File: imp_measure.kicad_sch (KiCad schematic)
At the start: 46 parts, among them IC1 DAC80501ZDGST, IC2 MAX660MX_NOPB, J1 Conn_01x04_Pin, J2 USB_B_Micro, J3 Conn_01x06_Pin, J4 Conn_01x06_Pin, SW1 SW_SPDT, U1 AMS1117-3.3, U2 STM32F401RCTx, U3 OPA196xDBV, Y1 26MHz

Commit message: PCB design 1.0
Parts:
- removed J3: Conn_01x06_Pin, Connector_PinHeader_2.54mm:PinHeader_1x04_P2.54mm_Vertical, symbol Connector:Conn_01x06_Pin
- removed U3: OPA196xDBV, Package_TO_SOT_SMD:SOT-23-5, symbol Amplifier_Operational:OPA196xDBV
- removed Y1: 26MHz, Crystal:Crystal_SMD_3225-4Pin_3.2x2.5mm, symbol Device:Crystal_GND23
- added C25: 100n, Capacitor_SMD:C_0805_2012Metric, symbol Device:C
- added C26, C27, C28, C30, C31: 1u, Capacitor_SMD:C_0805_2012Metric, symbol Device:C
- added C32: 10n, Capacitor_SMD:C_0805_2012Metric, symbol Device:C
- added FB3, FB4: 120R, Inductor_SMD:L_0805_2012Metric, symbol Device:FerriteBead
- added H1, H2, H3, H4: MountingHole, MountingHole:MountingHole_2mm, symbol Mechanical:MountingHole
- added IC4: MC33202DR2G, SamacSys_Parts:SOIC127P600X175-8N, symbol SamacSys_Parts:MC33202DR2G
- added J3, J5: Conn_01x04_Pin, Connector_PinHeader_2.54mm:PinHeader_1x04_P2.54mm_Vertical, symbol Connector:Conn_01x04_Pin
- added R9: 1k, Resistor_SMD:R_0805_2012Metric, symbol Device:R
- added Y1: Crystal, Crystal:Crystal_HC49-U_Vertical, symbol Device:Crystal
- C10, C11, C12, C13, C14, C15, C16, C17, C21, C22, C23, C4, C8, C9: footprint Capacitor_SMD:C_0402_1005Metric -> Capacitor_SMD:C_0805_2012Metric
- C18: value 100n -> 5n; footprint Capacitor_SMD:C_0402_1005Metric -> Capacitor_SMD:C_0805_2012Metric
- C19: value 100n -> 10n; footprint Capacitor_SMD:C_0402_1005Metric -> Capacitor_SMD:C_0805_2012Metric
- C3, C6, C7: footprint Capacitor_SMD:C_0603_1608Metric -> Capacitor_SMD:C_0805_2012Metric
- C5: value 100n -> 220n; footprint Capacitor_SMD:C_0402_1005Metric -> Capacitor_SMD:C_0805_2012Metric
- D1: footprint LED_SMD:LED_0603_1608Metric -> LED_SMD:LED_0805_2012Metric
- FB1, FB2: footprint Inductor_SMD:L_0603_1608Metric -> Inductor_SMD:L_0805_2012Metric
- R1, R2, R3, R4, R5: footprint Resistor_SMD:R_0402_1005Metric -> Resistor_SMD:R_0805_2012Metric
- R6, R7: value R -> 3k3; footprint Resistor_SMD:R_0402_1005Metric -> Resistor_SMD:R_0805_2012Metric
- R8: value R -> 1k6; footprint Resistor_SMD:R_0402_1005Metric -> Resistor_SMD:R_0805_2012Metric
- SW1: footprint Button_Switch_THT:SW_Slide_SPDT_Straight_CK_OS102011MS2Q -> Button_Switch_SMD:SW_SPDT_PCM12
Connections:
- net +3.3V: now also FB4.2; no longer C3.1, C4.1, C5.1, IC1.1 (VDD), IC1.10 (VREFIO)
- net +3.3VA: now also R9.1
- net ADC1_IN4: now also J3.3 (Pin_3)
- net ADC1_IN5: now also J3.2 (Pin_2)
- net DAC_OUT: now also J5.2 (Pin_2)
- net DAC_OUT_FILTERED: now also IC4.7 (OUTPUT_2), J5.3 (Pin_3)
- net GND: now also C27.2, C28.2, C30.2, C31.2, C32.2, IC4.3 (INPUTS_1_2), IC4.5 (INPUTS_2_1), J3.4 (Pin_4), J5.4 (Pin_4)
- net RCC_OSC_IN: now also Y1.1
- net RCC_OSC_OUT: now also Y1.2
- net VBUS: now also C3.1, C4.1, IC1.1 (VDD), C30.1, FB3.2
- net VBUS_M: now also C27.1
- net VBUS_MF: now also C25.2, IC4.4 (VEE)
- net at C18.1, R8.2: now also IC4.6 (INPUTS_2_2)
- net at C20.1, IC2.2 (CAP+): now also C26.1
- net at C20.2, IC2.4 (CAP-): now also C26.2
- new net: C5.1, IC1.10 (VREFIO), R9.2
- new net: IC4.1 (OUTPUT_1), IC4.2 (INPUTS_1_1)
- new net +3.3V_F: C28.1, FB4.1, J3.1 (Pin_1), J5.1 (Pin_1)
- new net VBUS_PF: C25.1, C31.1, C32.1, FB3.1, IC4.8 (VCC)
- no-connect marks 45 -> 44
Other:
- note added: "Butterworth low-pass"
- note added: "G(s) = -3787878787.8788/(s^2+123106.06s+3787878787.87788)"
- note added: "Mounting holes"
- note added: "VDDA filtering for OPAMP"
- note removed: "Butterworth low-pass components to be calculated"
- note removed: "Output stage?"
- moved on the sheet: C18, C19, C20, C21, C22, C23, C24, C3, C4, FB2, IC1, IC2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

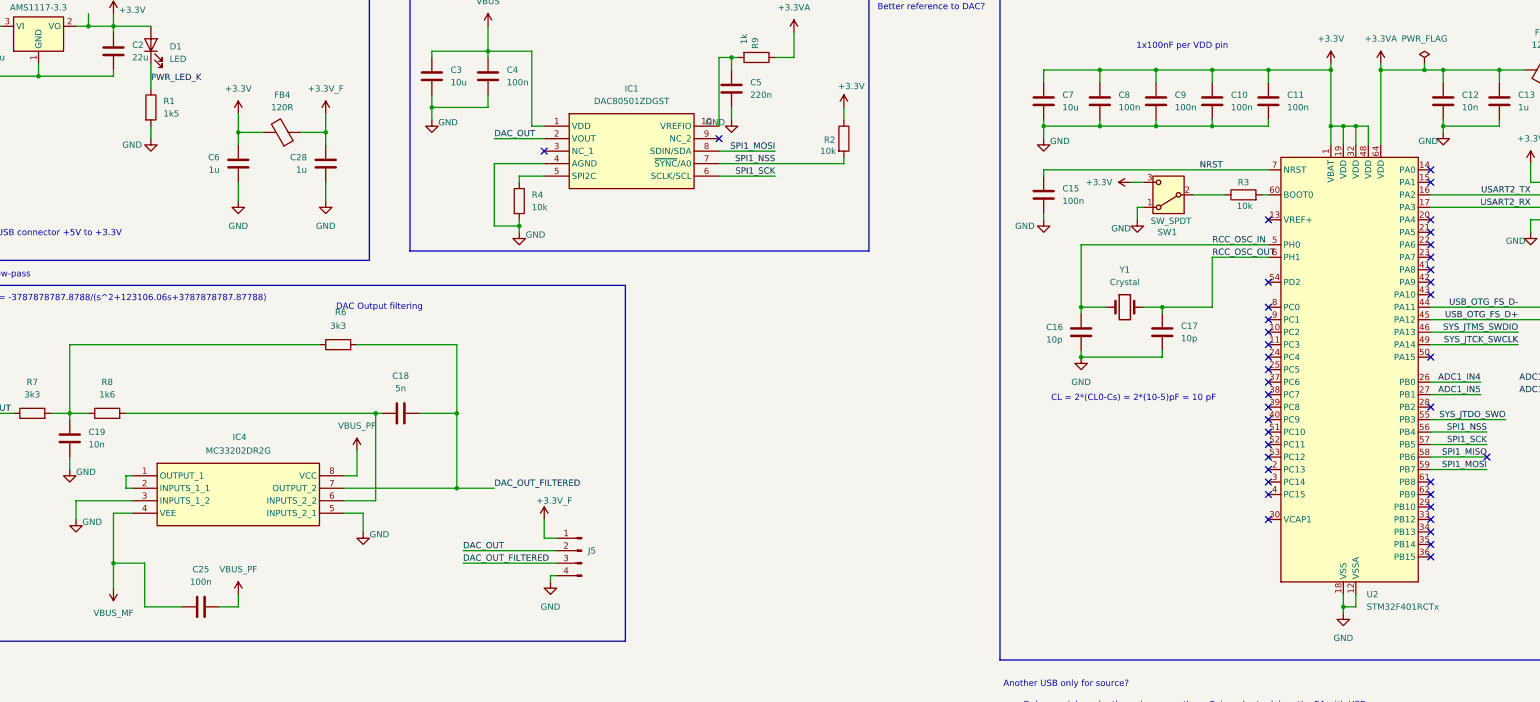
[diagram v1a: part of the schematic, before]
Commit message: Ground fill for analog part
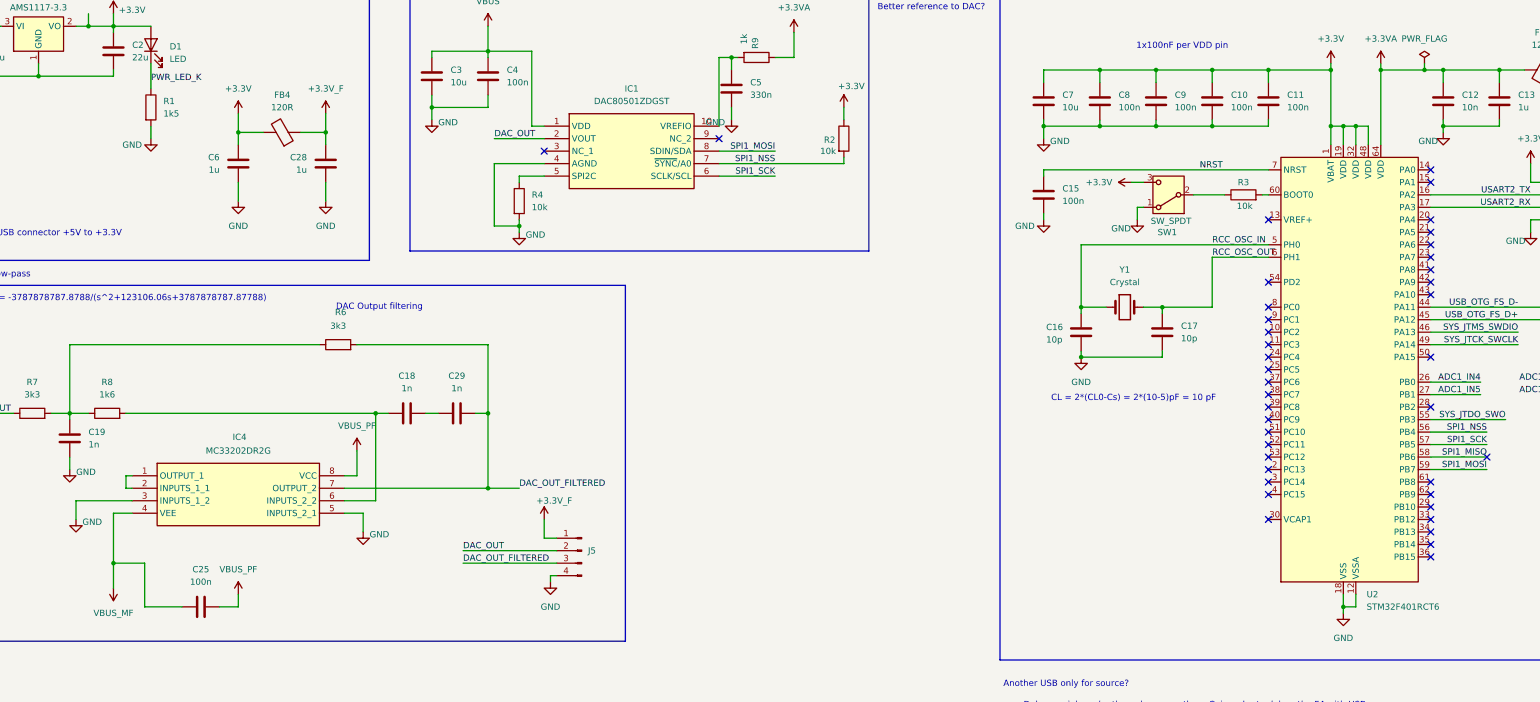
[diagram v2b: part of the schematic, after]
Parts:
- added C29: 1n, Capacitor_SMD:C_0805_2012Metric, symbol Device:C
- C18: value 5n -> 1n
- C19: value 10n -> 1n
- C5: value 220n -> 330n
- SW1: footprint Button_Switch_SMD:SW_SPDT_PCM12 -> Button_Switch_THT:SW_Slide-03_Wuerth-WS-SLTV_10x2.5x6.4_P2.54mm
- U2: value STM32F401RCTx -> STM32F401RCT6
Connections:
- net DAC_OUT_FILTERED: now also C29.2; no longer C18.2
- new net: C18.2, C29.1
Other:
- moved on the sheet: C18
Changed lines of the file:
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@@
 	)
 	(junction
-		(at 124.46 107.95)
-		(diameter 0)
-		(color 0 0 0 0)
-	)
-	(junction
 		(at 304.8 49.53)
 		(diameter 0)
@@
 	)
 	(junction
-		(at 151.13 194.31)
+		(at 130.81 123.19)
 		(diameter 0)
 		(color 0 0 0 0)
 	)
 	(junction
-		(at 255.27 38.1)
+		(at 151.13 194.31)
 		(diameter 0)
 		(color 0 0 0 0)
 	)
 	(junction
-		(at 82.55 196.85)
+		(at 255.27 38.1)
 		(diameter 0)
 		(color 0 0 0 0)
 	)
 	(junction
-		(at 124.46 123.19)
+		(at 82.55 196.85)
 		(diameter 0)
 		(color 0 0 0 0)
@@
 		(color 0 0 0 0)
 	)
+	(junction
+		(at 130.81 107.95)
+		(diameter 0)
+		(color 0 0 0 0)
+	)
 	(no_connect
 		(at 289.56 88.9)
@@
 	(wire
 		(pts
+			(xy 118.11 107.95) (xy 120.65 107.95)
+		)
+		(stroke
+			(width 0)
+			(type default)
+		)
+	)
+	(wire
+		(pts
 			(xy 353.06 107.95) (xy 353.06 106.68)
 		)
@@
 	(wire
 		(pts
-			(xy 107.95 107.95) (xy 109.22 107.95)
+			(xy 107.95 107.95) (xy 110.49 107.95)
 		)
 		(stroke
@@
 	(wire
 		(pts
-			(xy 101.6 123.19) (xy 124.46 123.19)
-		)
-		(stroke
-			(width 0)
-			(type default)
-		)
-	)
-	(wire
-		(pts
 			(xy 139.7 226.06) (xy 134.62 226.06)
 		)
@@
 	(wire
 		(pts
-			(xy 124.46 107.95) (xy 124.46 123.19)
+			(xy 130.81 93.98) (xy 130.81 107.95)
+		)
+		(stroke
+			(width 0)
+			(type default)
+		)
+	)
+	(wire
+		(pts
+			(xy 130.81 123.19) (xy 137.16 123.19)
 		)
 		(stroke
@@
 	(wire
 		(pts
-			(xy 124.46 123.19) (xy 132.08 123.19)
+			(xy 101.6 123.19) (xy 130.81 123.19)
 		)
 		(stroke
@@
 	(wire
 		(pts
+			(xy 130.81 107.95) (xy 130.81 123.19)
+		)
+		(stroke
+			(width 0)
+			(type default)
+		)
+	)
+	(wire
+		(pts
 			(xy 151.13 209.55) (xy 163.83 209.55)
 		)
@@
 	(wire
 		(pts
-			(xy 124.46 93.98) (xy 124.46 107.95)
-		)
-		(stroke
-			(width 0)
-			(type default)
-		)
-	)
-	(wire
-		(pts
 			(xy 177.8 54.61) (xy 189.23 54.61)
 		)
@@
 	(wire
 		(pts
-			(xy 368.3 83.82) (xy 363.22 83.82)
+			(xy 128.27 107.95) (xy 130.81 107.95)
 		)
 		(stroke
@@
 	(wire
 		(pts
-			(xy 118.11 209.55) (xy 121.92 209.55)
+			(xy 368.3 83.82) (xy 363.22 83.82)
 		)
 		(stroke
@@
 	(wire
 		(pts
-			(xy 266.7 49.53) (xy 255.27 49.53)
+			(xy 118.11 209.55) (xy 121.92 209.55)
 		)
 		(stroke
@@
 	(wire
 		(pts
-			(xy 307.34 53.34) (xy 307.34 49.53)
+			(xy 266.7 49.53) (xy 255.27 49.53)
 		)
 		(stroke
@@
 	(wire
 		(pts
-			(xy 116.84 107.95) (xy 124.46 107.95)
+			(xy 307.34 53.34) (xy 307.34 49.53)
 		)
 		(stroke
@@
 	(wire
 		(pts
-			(xy 104.14 93.98) (xy 124.46 93.98)
+			(xy 104.14 93.98) (xy 130.81 93.98)
 		)
 		(stroke
@@
 	)
 	(label "DAC_OUT_FILTERED"
-		(at 132.08 123.19 0)
+		(at 137.16 123.19 0)
 		(fields_autoplaced yes)
 		(effects
@@
 		(on_board yes)
 		(dnp no)
-		(fields_autoplaced yes)
 		(property "Reference" "C15"
 			(at 247.65 62.2299 0)
@@
 			)
 		)
-		(property "Value" "STM32F401RCTx"
+		(property "Value" "STM32F401RCT6"
 			(at 309.5341 147.32 0)
 			(effects
@@
 			)
 		)
-		(property "Footprint" "Button_Switch_SMD:SW_SPDT_PCM12"
+		(property "Footprint" "Button_Switch_THT:SW_Slide-03_Wuerth-WS-SLTV_10x2.5x6.4_P2.54mm"
 			(at 269.24 63.5 0)
 			(effects
@@
 			)
 		)
-		(property "Value" "10n"
+		(property "Value" "1n"
 			(at 49.53 114.2999 0)
 			(effects
@@
 	(symbol
 		(lib_id "Device:C")
+		(at 124.46 107.95 90)
+		(unit 1)
+		(exclude_from_sim no)
+		(in_bom yes)
+		(on_board yes)
+		(dnp no)
+		(fields_autoplaced yes)
+		(property "Reference" "C29"
+			(at 124.46 100.33 90)
+			(effects
+				(font
+					(size 1.27 1.27)
+				)
+			)
+		)
+		(property "Value" "1n"
+			(at 124.46 102.87 90)
+			(effects
+				(font
+					(size 1.27 1.27)
+				)
+			)
+		)
+		(property "Footprint" "Capacitor_SMD:C_0805_2012Metric"
+			(at 128.27 106.9848 0)
+			(effects
+				(font
+					(size 1.27 1.27)
+				)
+				(hide yes)
+			)
+		)
+		(property "Datasheet" "~"
+			(at 124.46 107.95 0)
+			(effects
+				(font
+					(size 1.27 1.27)
+				)
+				(hide yes)
+			)
+		)
+		(property "Description" "Unpolarized capacitor"
+			(at 124.46 107.95 0)
+			(effects
+				(font
+					(size 1.27 1.27)
+				)
+				(hide yes)
+			)
+		)
+		(pin "2"
+		)
+		(pin "1"
+		)
+		(instances
+			(project "imp_measure"
+				(path "/1fe94d98-d50f-4985-8f0a-d51e6882779a"
+					(reference "C29")
+					(unit 1)
+				)
+			)
+		)
+	)
+	(symbol
+		(lib_id "Device:C")
 		(at 266.7 44.45 0)
 		(unit 1)
@@
 	(symbol
 		(lib_id "Device:C")
-		(at 113.03 107.95 90)
+		(at 114.3 107.95 90)
 		(unit 1)
 		(exclude_from_sim no)
@@
 		(fields_autoplaced yes)
 		(property "Reference" "C18"
-			(at 113.03 100.33 90)
+			(at 114.3 100.33 90)
 			(effects
 				(font
@@
 			)
 		)
-		(property "Value" "5n"
-			(at 113.03 102.87 90)
+		(property "Value" "1n"
+			(at 114.3 102.87 90)
 			(effects
 				(font
@@
 		)
 		(property "Footprint" "Capacitor_SMD:C_0805_2012Metric"
-			(at 116.84 106.9848 0)
+			(at 118.11 106.9848 0)
 			(effects
 				(font
@@
 		)
 		(property "Datasheet" "~"
-			(at 113.03 107.95 0)
+			(at 114.3 107.95 0)
 			(effects
 				(font
@@
 		)
 		(property "Description" "Unpolarized capacitor"
-			(at 113.03 107.95 0)
+			(at 114.3 107.95 0)
 			(effects
 				(font
@@
 			)
 		)
-		(property "Value" "220n"
+		(property "Value" "330n"
 			(at 184.15 43.1799 0)
 			(effects

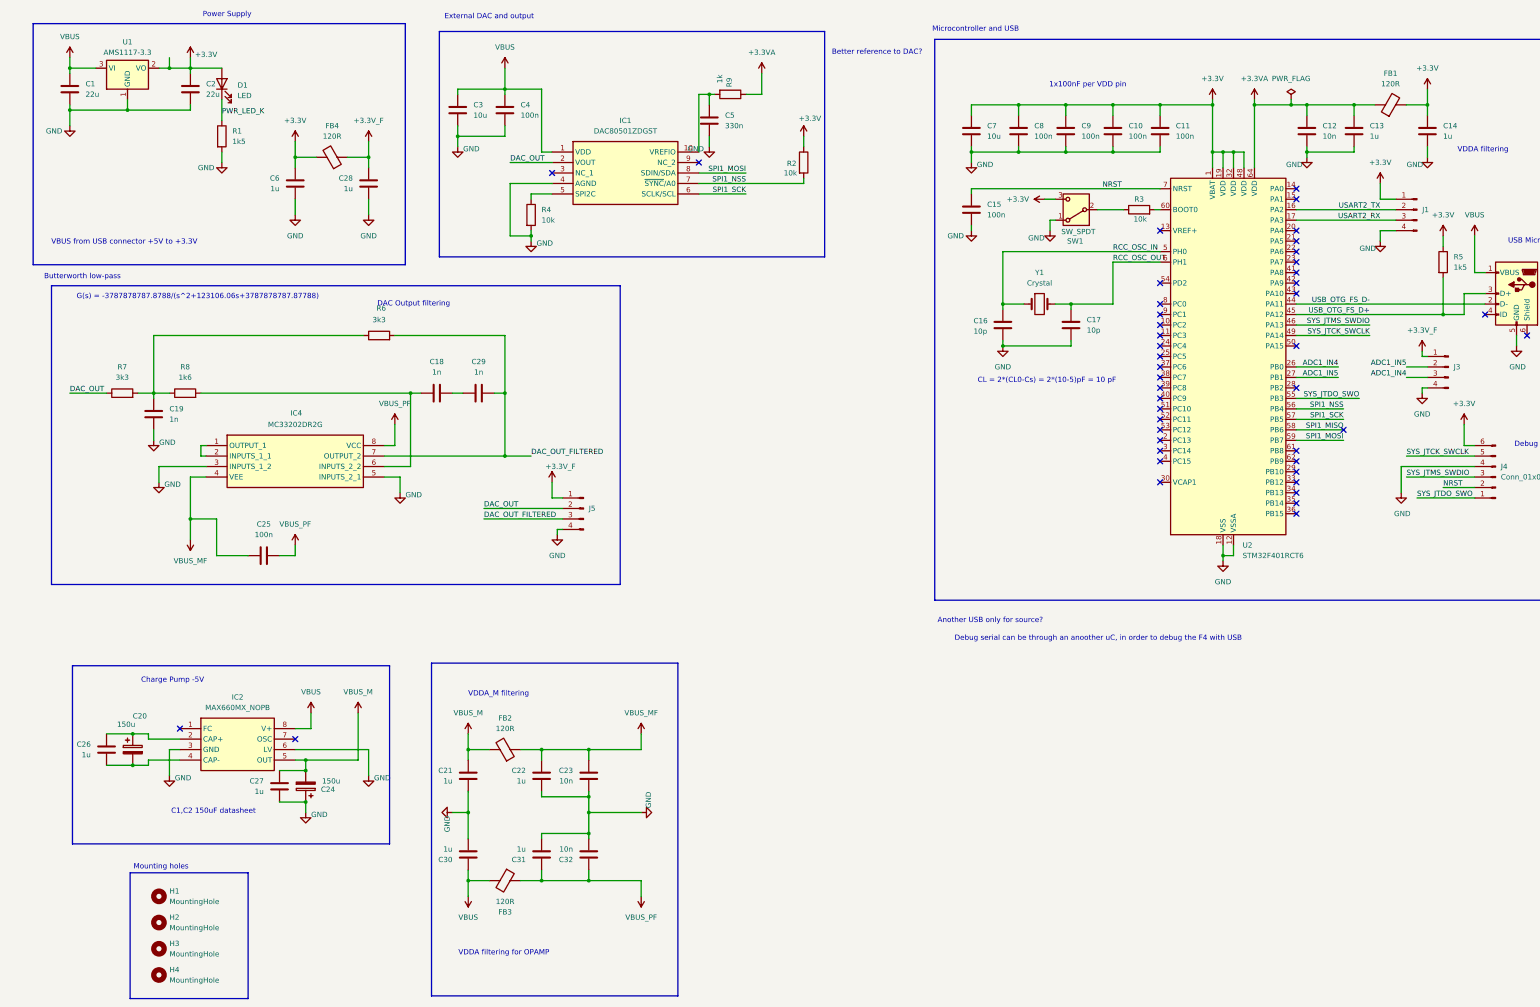
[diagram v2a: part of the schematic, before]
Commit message: PCB v1.2
Changing the Multiple Feedback topology to Salen-Key.
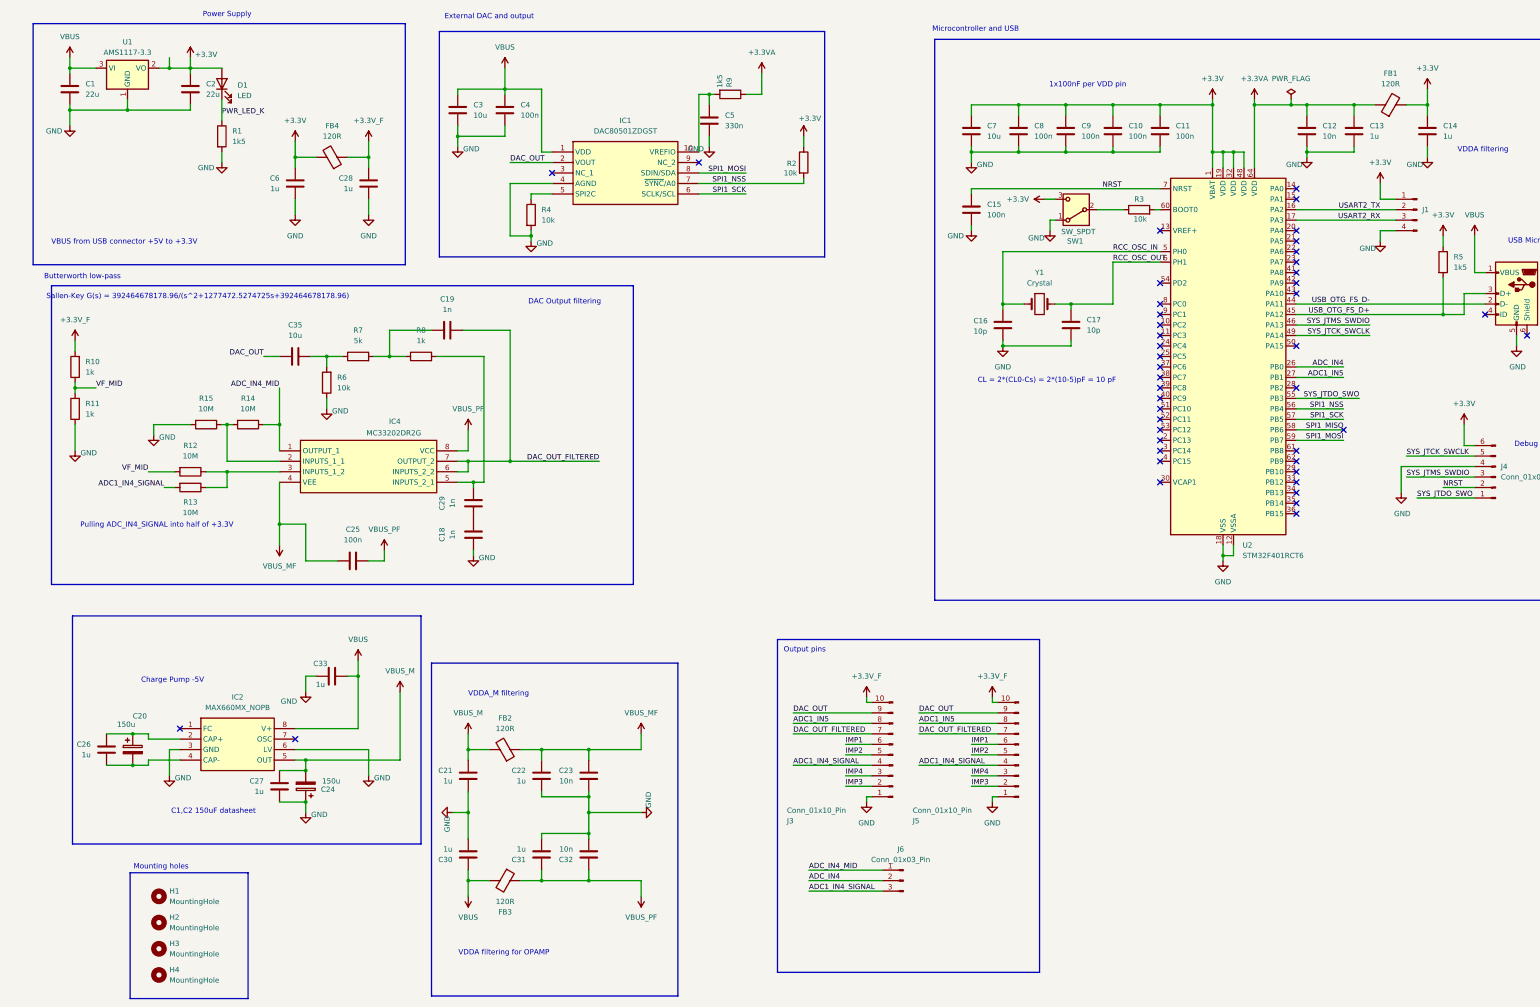
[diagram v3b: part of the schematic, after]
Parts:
- removed J3, J5: Conn_01x04_Pin, Connector_PinHeader_2.54mm:PinHeader_1x04_P2.54mm_Vertical, symbol Connector:Conn_01x04_Pin
- added C33: 1u, Capacitor_SMD:C_0805_2012Metric, symbol Device:C
- added C35: 10u, Capacitor_SMD:C_0805_2012Metric, symbol Device:C
- added J3, J5: Conn_01x10_Pin, Connector_PinSocket_2.54mm:PinSocket_1x10_P2.54mm_Vertical, symbol Connector:Conn_01x10_Pin
- added J6: Conn_01x03_Pin, Connector_PinHeader_2.54mm:PinHeader_1x03_P2.54mm_Vertical, symbol Connector:Conn_01x03_Pin
- added R10, R11: 1k, Resistor_SMD:R_0805_2012Metric, symbol Device:R
- added R12, R13, R14, R15: 10M, Resistor_SMD:R_0805_2012Metric, symbol Device:R
- R6: value 3k3 -> 10k
- R7: value 3k3 -> 5k
- R8: value 1k6 -> 1k
- R9: value 1k -> 1k5
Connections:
- net +3.3V_F: now also J3.10 (Pin_10), J5.10 (Pin_10), R10.2
- net ADC1_IN5: now also J3.8 (Pin_8), J5.8 (Pin_8)
- net DAC_OUT: now also C35.1, J3.9 (Pin_9), J5.9 (Pin_9); no longer R7.1
- net DAC_OUT_FILTERED: now also C19.2, IC4.6 (INPUTS_2_2), J3.7 (Pin_7), J5.7 (Pin_7); no longer C29.2, R6.2
- net GND: now also C18.1, R6.1, C33.1, J3.1 (Pin_1), J5.1 (Pin_1), R11.1, R15.2; no longer C19.2, IC4.3 (INPUTS_1_2), IC4.5 (INPUTS_2_1)
- net VBUS: now also C33.2
- net at C19.1, R7.2, R8.1: no longer R6.1
- net at IC4.2 (INPUTS_1_1): now also R14.2, R15.1; no longer IC4.1 (OUTPUT_1)
- net ADC1_IN4 renamed ADC_IN4
- net ADC_IN4: now also J6.2 (Pin_2)
- new net: C35.2, R6.2, R7.1
- new net: C29.2, IC4.5 (INPUTS_2_1), R8.2
- new net: IC4.3 (INPUTS_1_2), R12.1, R13.1
- new net ADC1_IN4_SIGNAL: J3.4 (Pin_4), J5.4 (Pin_4), J6.3 (Pin_3), R13.2
- new net ADC_IN4_MID: IC4.1 (OUTPUT_1), J6.1 (Pin_1), R14.1
- new net IMP1: J3.6 (Pin_6), J5.6 (Pin_6)
- new net IMP2: J3.5 (Pin_5), J5.5 (Pin_5)
- new net IMP3: J3.2 (Pin_2), J5.2 (Pin_2)
- new net IMP4: J3.3 (Pin_3), J5.3 (Pin_3)
- new net VF_MID: R10.1, R11.2, R12.2
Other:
- note added: "Output pins"
- note added: "Pulling ADC_IN4_SIGNAL into half of +3.3V"
- note added: "Sallen-Key G(s) = 392464678178.96/(s^2+1277472.5274725s+392464678178.96)"
- note removed: "Another USB only for source?"
- note removed: "Better reference to DAC?"
- note removed: "Debug serial can be through an anoother uC, in order to debug the F4 with USB"
- note removed: "G(s) = -3787878787.8788/(s^2+123106.06s+3787878787.87788)"
- moved on the sheet: C18, C19, C25, C29, IC4, R7, R8
